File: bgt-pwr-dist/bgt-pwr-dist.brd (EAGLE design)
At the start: 40 x 100 mm, 30 parts

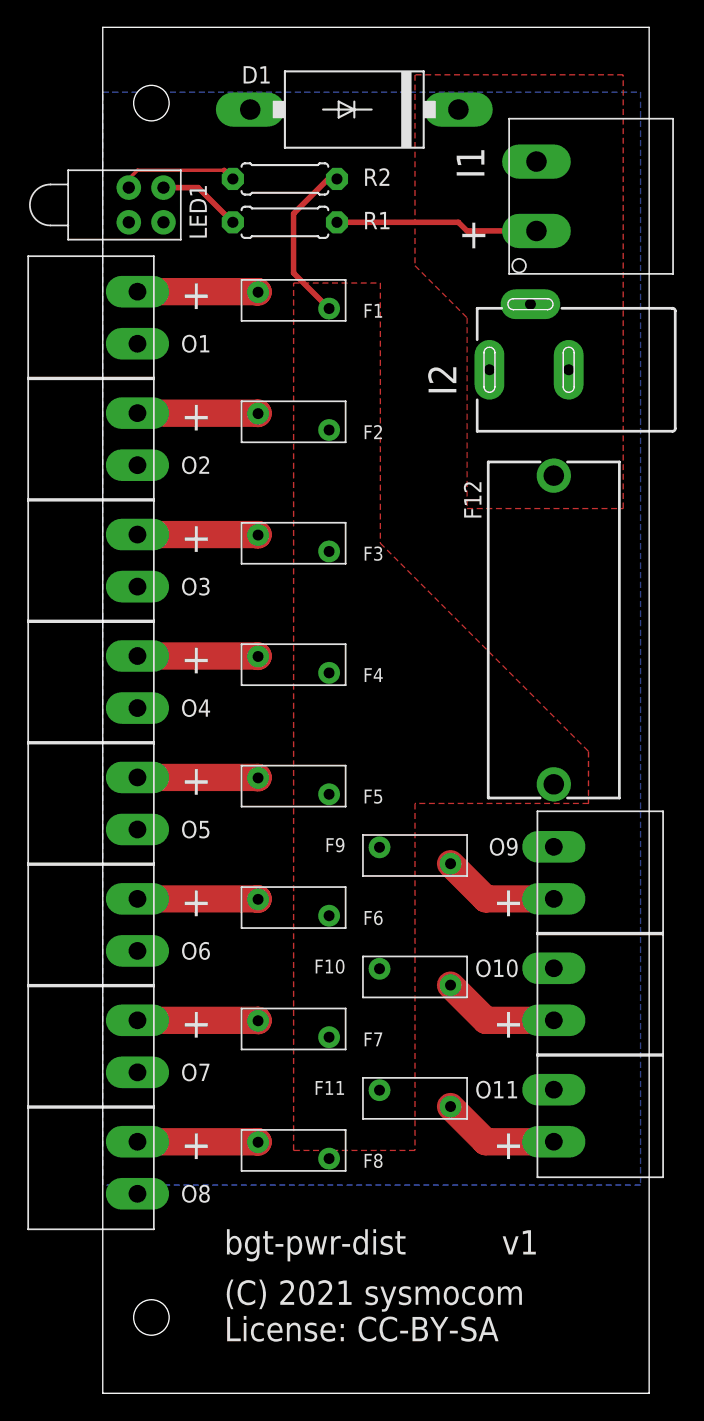
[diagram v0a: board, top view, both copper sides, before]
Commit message: bgt-prw-dist: various small fixes
* update littelfuse library for 0.9mm drill (instead of 0.8mm)
* increase restring sizes
* increase trace width from 2mm to 2.54mm
* 10mm THT resistor instead of 7mm
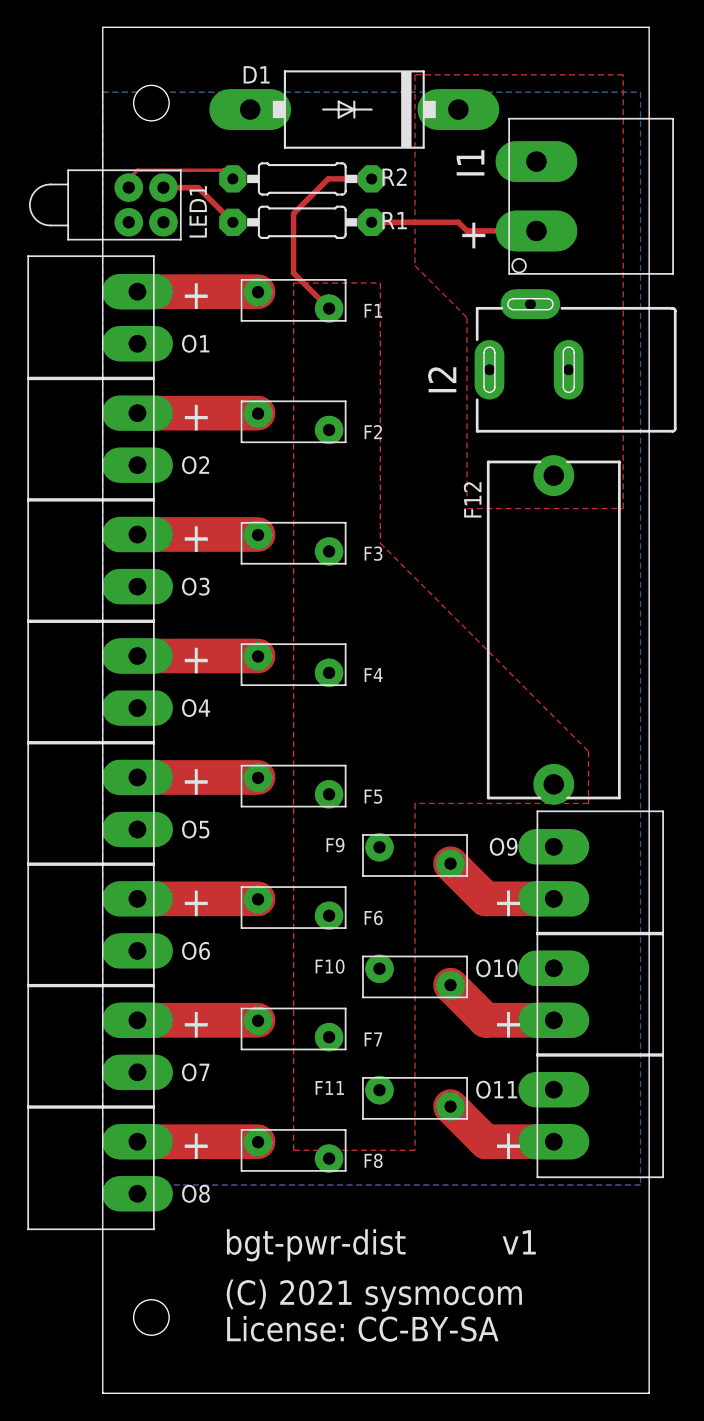
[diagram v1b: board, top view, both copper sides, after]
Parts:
- R1, R2: device resistor:0207/7 -> resistor:0207/10
- moved R1 1.27 mm to (14.6, 85.7)
- moved R2 1.27 mm to (14.6, 88.9)
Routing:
- net VIN: track 14.9 -> 12.3 mm
- net VCC: track 12.3 -> 14.8 mm
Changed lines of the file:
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@@
 <param name="rvMicroViaOuter" value="0.25"/>
 <param name="rvMicroViaInner" value="0.25"/>
-<param name="rlMinPadTop" value="0.25mm"/>
-<param name="rlMaxPadTop" value="20mil"/>
+<param name="rlMinPadTop" value="0.6mm"/>
+<param name="rlMaxPadTop" value="0.8mm"/>
 <param name="rlMinPadInner" value="10mil"/>
 <param name="rlMaxPadInner" value="20mil"/>
@@
 <attribute name="NAME" x="7.62" y="84.455" size="1.27" layer="25" rot="R90"/>
 </element>
-<element name="R1" library="resistor" package="0207/7" value="" x="13.335" y="85.725" smashed="yes">
-<attribute name="NAME" x="19.05" y="85.217" size="1.27" layer="25" ratio="10"/>
-<attribute name="VALUE" x="11.049" y="85.1662" size="1.27" layer="27" ratio="10"/>
-</element>
-<element name="R2" library="resistor" package="0207/7" value="" x="13.335" y="88.9" smashed="yes">
-<attribute name="NAME" x="19.05" y="88.392" size="1.27" layer="25" ratio="10"/>
-<attribute name="VALUE" x="11.049" y="88.3412" size="1.27" layer="27" ratio="10"/>
+<element name="R1" library="resistor" package="0207/10" value="" x="14.605" y="85.725" smashed="yes">
+<attribute name="NAME" x="20.32" y="85.217" size="1.27" layer="25" ratio="10"/>
+<attribute name="VALUE" x="12.319" y="85.1662" size="1.27" layer="27" ratio="10"/>
+</element>
+<element name="R2" library="resistor" package="0207/10" value="" x="14.605" y="88.9" smashed="yes">
+<attribute name="NAME" x="20.32" y="88.392" size="1.27" layer="25" ratio="10"/>
+<attribute name="VALUE" x="12.319" y="88.3412" size="1.27" layer="27" ratio="10"/>
 </element>
 </elements>
@@
 <contactref element="O1" pad="1"/>
 <contactref element="F1" pad="1"/>
-<wire x1="2.54" y1="80.645" x2="11.37" y2="80.645" width="2" layer="1"/>
+<wire x1="2.54" y1="80.645" x2="11.37" y2="80.645" width="2.54" layer="1"/>
 <wire x1="11.37" y1="80.645" x2="11.37" y2="80.61" width="2" layer="1"/>
 </signal>
@@
 <contactref element="O2" pad="1"/>
 <contactref element="F2" pad="1"/>
-<wire x1="2.54" y1="71.755" x2="11.37" y2="71.755" width="2" layer="1"/>
+<wire x1="2.54" y1="71.755" x2="11.37" y2="71.755" width="2.54" layer="1"/>
 <wire x1="11.37" y1="71.755" x2="11.37" y2="71.72" width="2" layer="1"/>
 </signal>
@@
 <contactref element="O3" pad="1"/>
 <contactref element="F3" pad="1"/>
-<wire x1="2.54" y1="62.865" x2="11.37" y2="62.865" width="2" layer="1"/>
+<wire x1="2.54" y1="62.865" x2="11.37" y2="62.865" width="2.54" layer="1"/>
 <wire x1="11.37" y1="62.865" x2="11.37" y2="62.83" width="2" layer="1"/>
 </signal>
@@
 <contactref element="O4" pad="1"/>
 <contactref element="F4" pad="1"/>
-<wire x1="2.54" y1="53.975" x2="11.37" y2="53.975" width="2" layer="1"/>
+<wire x1="2.54" y1="53.975" x2="11.37" y2="53.975" width="2.54" layer="1"/>
 <wire x1="11.37" y1="53.975" x2="11.37" y2="53.94" width="2" layer="1"/>
 </signal>
@@
 <contactref element="O5" pad="1"/>
 <contactref element="F5" pad="1"/>
-<wire x1="2.54" y1="45.085" x2="11.37" y2="45.085" width="2" layer="1"/>
+<wire x1="2.54" y1="45.085" x2="11.37" y2="45.085" width="2.54" layer="1"/>
 <wire x1="11.37" y1="45.085" x2="11.37" y2="45.05" width="2" layer="1"/>
 </signal>
@@
 <contactref element="O6" pad="1"/>
 <contactref element="F6" pad="1"/>
-<wire x1="2.54" y1="36.195" x2="11.37" y2="36.195" width="2" layer="1"/>
+<wire x1="2.54" y1="36.195" x2="11.37" y2="36.195" width="2.54" layer="1"/>
 <wire x1="11.37" y1="36.195" x2="11.37" y2="36.16" width="2" layer="1"/>
 </signal>
@@
 <contactref element="O7" pad="1"/>
 <contactref element="F7" pad="1"/>
-<wire x1="2.54" y1="27.305" x2="11.37" y2="27.305" width="2" layer="1"/>
+<wire x1="2.54" y1="27.305" x2="11.37" y2="27.305" width="2.54" layer="1"/>
 <wire x1="11.37" y1="27.305" x2="11.37" y2="27.27" width="2" layer="1"/>
 </signal>
@@
 <contactref element="O8" pad="1"/>
 <contactref element="F8" pad="1"/>
-<wire x1="2.54" y1="18.415" x2="11.37" y2="18.415" width="2" layer="1"/>
+<wire x1="2.54" y1="18.415" x2="11.37" y2="18.415" width="2.54" layer="1"/>
 <wire x1="11.37" y1="18.415" x2="11.37" y2="18.38" width="2" layer="1"/>
 </signal>
@@
 </polygon>
 <contactref element="R2" pad="2"/>
-<wire x1="17.145" y1="88.9" x2="16.51" y2="88.9" width="0.4064" layer="1"/>
+<wire x1="19.685" y1="88.9" x2="16.51" y2="88.9" width="0.4064" layer="1"/>
 <wire x1="16.51" y1="88.9" x2="13.97" y2="86.36" width="0.4064" layer="1"/>
 <wire x1="13.97" y1="86.36" x2="13.97" y2="82.01" width="0.4064" layer="1"/>
@@
 <vertex x="38.1" y="96.52"/>
 </polygon>
-<wire x1="17.145" y1="85.725" x2="26.035" y2="85.725" width="0.4064" layer="1"/>
+<wire x1="19.685" y1="85.725" x2="26.035" y2="85.725" width="0.4064" layer="1"/>
 <wire x1="26.035" y1="85.725" x2="26.67" y2="85.09" width="0.4064" layer="1"/>
 <wire x1="26.67" y1="85.09" x2="31.75" y2="85.09" width="0.4064" layer="1"/>
@@
 <contactref element="O9" pad="1"/>
 <contactref element="F9" pad="1"/>
-<wire x1="33.02" y1="36.195" x2="28.035" y2="36.195" width="2" layer="1"/>
-<wire x1="28.035" y1="36.195" x2="25.46" y2="38.77" width="2" layer="1"/>
+<wire x1="33.02" y1="36.195" x2="28.035" y2="36.195" width="2.54" layer="1"/>
+<wire x1="28.035" y1="36.195" x2="25.46" y2="38.77" width="2.54" layer="1"/>
 </signal>
 <signal name="N$12">
 <contactref element="O10" pad="1"/>
 <contactref element="F10" pad="1"/>
-<wire x1="33.02" y1="27.305" x2="28.035" y2="27.305" width="2" layer="1"/>
-<wire x1="28.035" y1="27.305" x2="25.46" y2="29.88" width="2" layer="1"/>
+<wire x1="33.02" y1="27.305" x2="28.035" y2="27.305" width="2.54" layer="1"/>
+<wire x1="28.035" y1="27.305" x2="25.46" y2="29.88" width="2.54" layer="1"/>
 </signal>
 <signal name="N$13">
 <contactref element="O11" pad="1"/>
 <contactref element="F11" pad="1"/>
-<wire x1="33.02" y1="18.415" x2="28.035" y2="18.415" width="2" layer="1"/>
-<wire x1="28.035" y1="18.415" x2="25.46" y2="20.99" width="2" layer="1"/>
+<wire x1="33.02" y1="18.415" x2="28.035" y2="18.415" width="2.54" layer="1"/>
+<wire x1="28.035" y1="18.415" x2="25.46" y2="20.99" width="2.54" layer="1"/>
 </signal>
 <signal name="N$10" class="1">

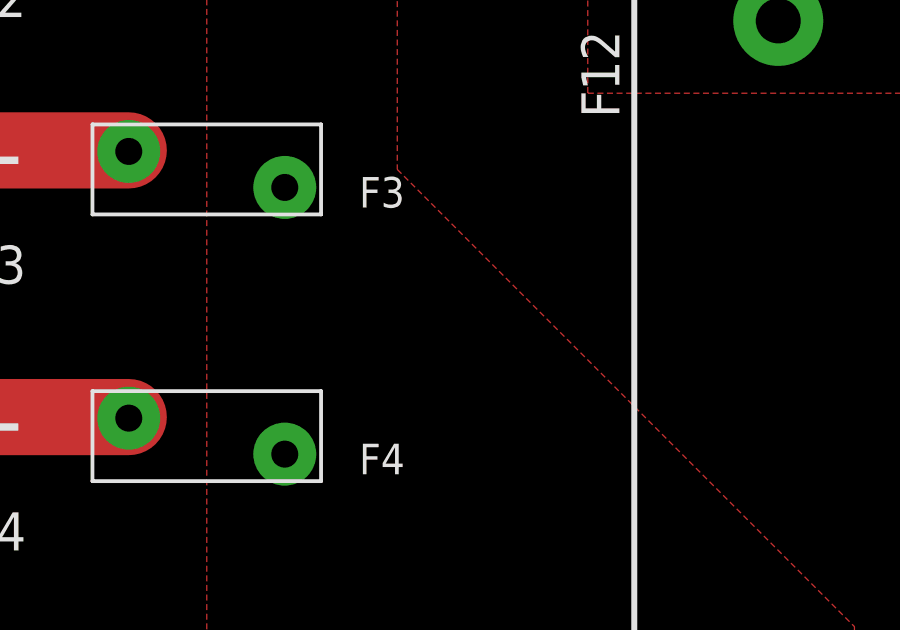
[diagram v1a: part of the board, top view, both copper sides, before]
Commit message: bgt-pwr-dist: cosmetics
* name / license / version on back side silk screen
* OSHW logo on silk screen
* polarity markers on back side silk screen
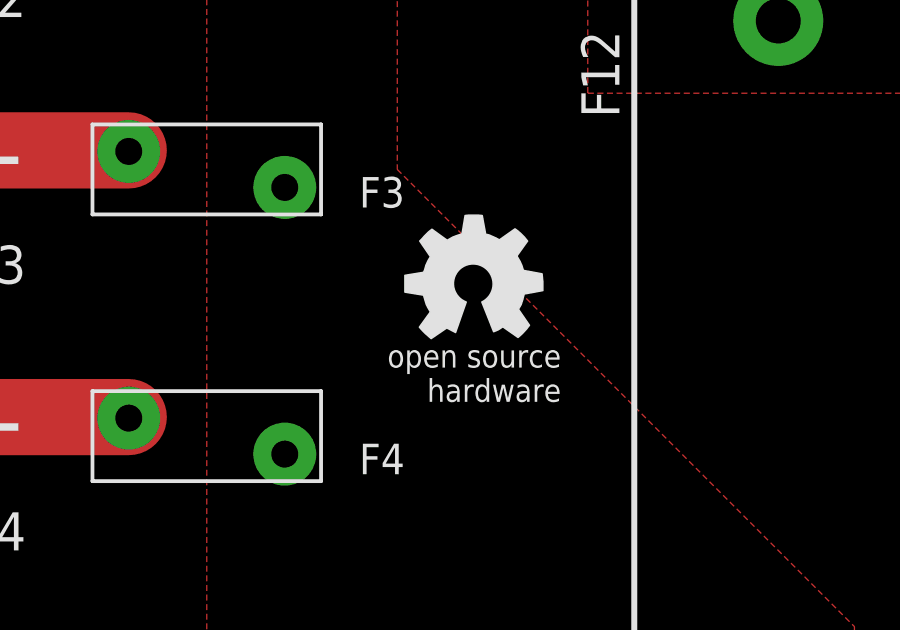
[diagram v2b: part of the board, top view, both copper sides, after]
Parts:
- added U$2, U$3: (no value), oshw:OSHW_5MM
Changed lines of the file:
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@@
 <layer number="48" name="Document" color="7" fill="1" visible="yes" active="yes"/>
 <layer number="49" name="Reference" color="7" fill="1" visible="yes" active="yes"/>
+<layer number="50" name="dxf" color="7" fill="1" visible="no" active="no"/>
 <layer number="51" name="tDocu" color="7" fill="1" visible="yes" active="yes"/>
 <layer number="52" name="bDocu" color="7" fill="1" visible="yes" active="yes"/>
+<layer number="53" name="tGND_GNDA" color="7" fill="9" visible="no" active="no"/>
+<layer number="54" name="bGND_GNDA" color="1" fill="9" visible="no" active="no"/>
+<layer number="56" name="wert" color="7" fill="1" visible="no" active="no"/>
 <layer number="90" name="Modules" color="5" fill="1" visible="no" active="no"/>
 <layer number="91" name="Nets" color="2" fill="1" visible="no" active="no"/>
@@
 <layer number="98" name="Guide" color="6" fill="1" visible="no" active="no"/>
 <layer number="99" name="SpiceOrder" color="5" fill="1" visible="no" active="no"/>
+<layer number="100" name="Muster" color="7" fill="1" visible="no" active="no"/>
+<layer number="101" name="Patch_Top" color="12" fill="4" visible="yes" active="yes"/>
+<layer number="102" name="Vscore" color="7" fill="1" visible="yes" active="yes"/>
+<layer number="103" name="tMap" color="7" fill="1" visible="yes" active="yes"/>
+<layer number="104" name="Name" color="7" fill="1" visible="yes" active="yes"/>
+<layer number="105" name="tPlate" color="7" fill="1" visible="yes" active="yes"/>
+<layer number="106" name="bPlate" color="7" fill="1" visible="yes" active="yes"/>
+<layer number="107" name="Crop" color="7" fill="1" visible="yes" active="yes"/>
+<layer number="116" name="Patch_BOT" color="9" fill="4" visible="yes" active="yes"/>
+<layer number="121" name="_tsilk" color="7" fill="1" visible="yes" active="yes"/>
+<layer number="122" name="_bsilk" color="7" fill="1" visible="yes" active="yes"/>
+<layer number="125" name="_tNames" color="7" fill="1" visible="yes" active="yes"/>
+<layer number="144" name="Drill_legend" color="7" fill="1" visible="yes" active="yes"/>
+<layer number="151" name="HeatSink" color="7" fill="1" visible="yes" active="yes"/>
+<layer number="200" name="200bmp" color="1" fill="10" visible="yes" active="yes"/>
+<layer number="201" name="201bmp" color="2" fill="1" visible="no" active="no"/>
+<layer number="202" name="202bmp" color="3" fill="1" visible="no" active="no"/>
+<layer number="203" name="203bmp" color="4" fill="10" visible="yes" active="yes"/>
+<layer number="204" name="204bmp" color="5" fill="10" visible="yes" active="yes"/>
+<layer number="205" name="205bmp" color="6" fill="10" visible="yes" active="yes"/>
+<layer number="206" name="206bmp" color="7" fill="10" visible="yes" active="yes"/>
+<layer number="207" name="207bmp" color="8" fill="10" visible="yes" active="yes"/>
+<layer number="208" name="208bmp" color="9" fill="10" visible="yes" active="yes"/>
+<layer number="209" name="209bmp" color="7" fill="1" visible="yes" active="yes"/>
+<layer number="210" name="210bmp" color="7" fill="1" visible="yes" active="yes"/>
+<layer number="211" name="211bmp" color="7" fill="1" visible="yes" active="yes"/>
+<layer number="212" name="212bmp" color="7" fill="1" visible="yes" active="yes"/>
+<layer number="213" name="213bmp" color="7" fill="1" visible="yes" active="yes"/>
+<layer number="214" name="214bmp" color="7" fill="1" visible="yes" active="yes"/>
+<layer number="215" name="215bmp" color="7" fill="1" visible="yes" active="yes"/>
+<layer number="216" name="216bmp" color="7" fill="1" visible="yes" active="yes"/>
+<layer number="250" name="Descript" color="3" fill="1" visible="no" active="no"/>
+<layer number="251" name="SMDround" color="12" fill="11" visible="no" active="no"/>
+<layer number="254" name="cooling" color="7" fill="1" visible="yes" active="yes"/>
 </layers>
 <board>
@@
 <text x="28.575" y="34.925" size="2.1844" layer="25" font="vector" ratio="14">+</text>
 <text x="26.035" y="83.82" size="2.1844" layer="25" font="vector" ratio="14">+</text>
+<text x="35.56" y="3.81" size="1.778" layer="26" font="vector" ratio="14" rot="MR0">(C) 2021 sysmocom
+License: CC-BY-SA</text>
+<text x="31.75" y="10.16" size="1.778" layer="26" font="vector" ratio="14" rot="MR0">bgt-pwr-dist</text>
+<text x="11.43" y="10.16" size="1.778" layer="26" font="vector" ratio="14" rot="MR0">&gt;VERSION</text>
+<text x="6.985" y="79.375" size="2.1844" layer="26" font="vector" ratio="14" rot="MR0">+</text>
+<text x="6.985" y="70.485" size="2.1844" layer="26" font="vector" ratio="14" rot="MR0">+</text>
+<text x="6.985" y="61.595" size="2.1844" layer="26" font="vector" ratio="14" rot="MR0">+</text>
+<text x="6.985" y="52.705" size="2.1844" layer="26" font="vector" ratio="14" rot="MR0">+</text>
+<text x="6.985" y="43.815" size="2.1844" layer="26" font="vector" ratio="14" rot="MR0">+</text>
+<text x="6.985" y="34.925" size="2.1844" layer="26" font="vector" ratio="14" rot="MR0">+</text>
+<text x="6.985" y="26.035" size="2.1844" layer="26" font="vector" ratio="14" rot="MR0">+</text>
+<text x="6.985" y="17.145" size="2.1844" layer="26" font="vector" ratio="14" rot="MR0">+</text>
+<text x="29.845" y="17.145" size="2.1844" layer="26" font="vector" ratio="14" rot="MR0">+</text>
+<text x="29.845" y="26.035" size="2.1844" layer="26" font="vector" ratio="14" rot="MR0">+</text>
+<text x="29.845" y="34.925" size="2.1844" layer="26" font="vector" ratio="14" rot="MR0">+</text>
+<text x="27.305" y="84.455" size="2.1844" layer="26" font="vector" ratio="14" rot="MR0">+</text>
 </plain>
 <attributes>
@@
 <attribute name="VALUE" x="12.319" y="88.3412" size="1.27" layer="27" ratio="10"/>
 </element>
+<element name="U$2" library="oshw" package="OSHW_5MM" value="" x="22.86" y="58.42"/>
+<element name="U$3" library="oshw" package="OSHW_5MM" value="" x="22.86" y="58.42" rot="MR0"/>
 </elements>
 <signals>
